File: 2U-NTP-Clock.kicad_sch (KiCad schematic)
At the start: 266 parts, among them Q1 BSS138, Q10 BSS138, Q11 BSS138, Q12 BSS138, Q13 BSS138, Q14 BSS138, Q15 BSS138, Q16 BSS138, Q17 BSS138, Q18 BSS138, Q19 BSS138, Q2 BSS138, Q20 BSS138, Q21 BSS138, Q22 BSS138, Q23 BSS138, Q24 BSS138, Q25 BSS138, Q26 BSS138, Q27 BSS138, Q28 BSS138, Q29 BSS138, Q3 BSS138, Q30 BSS138, Q31 BSS138, Q32 BSS138, Q33 BSS138, Q34 BSS138, Q35 BSS138, Q36 BSS138, Q37 BSS138, Q38 BSS138, Q39 BSS138, Q4 BSS138, Q40 BSS138, Q41 BSS138, Q42 BSS138, Q43 BSS138, Q5 BSS138, Q6 BSS138, Q7 BSS138, Q8 BSS138, Q9 BSS138, U3 74HC595, U4 74HC595, U5 74HC595, U6 74HC595, U7 74HC595, U8 74HC595

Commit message: 仕上げた
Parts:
- added C1: 0.22u, Capacitor_SMD:C_0603_1608Metric, symbol Device:C
- added C2: 0.1u, Capacitor_SMD:C_0603_1608Metric, symbol Device:C
- added D173: D, Diode_SMD:D_SOD-523, symbol Device:D
- added J1: Barrel_Jack_Switch, Connector_BarrelJack:BarrelJack_Horizontal, symbol Connector:Barrel_Jack_Switch
- added U9: L7805, Package_TO_SOT_SMD:TO-252-2, symbol Regulator_Linear:L7805
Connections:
- net +5V: now also C2.1, D173.2 (A), U9.3 (OUT)
- net GND: now also C1.2, C2.2, J1.2, U9.2 (GND)
- new net +12V: C1.1, D173.1 (K), J1.1, J1.3, U9.1 (IN)

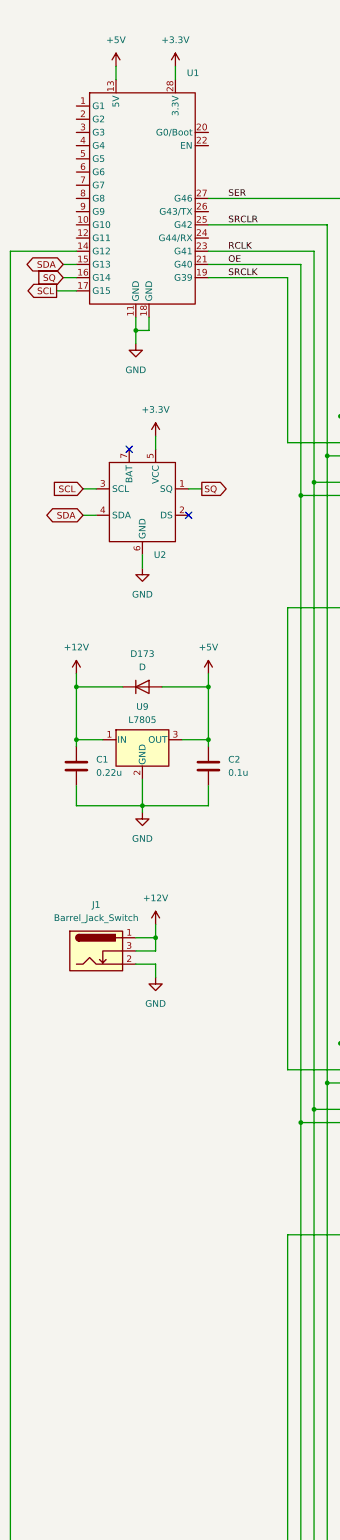
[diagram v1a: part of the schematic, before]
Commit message: スイッチの追加と配置配線修正
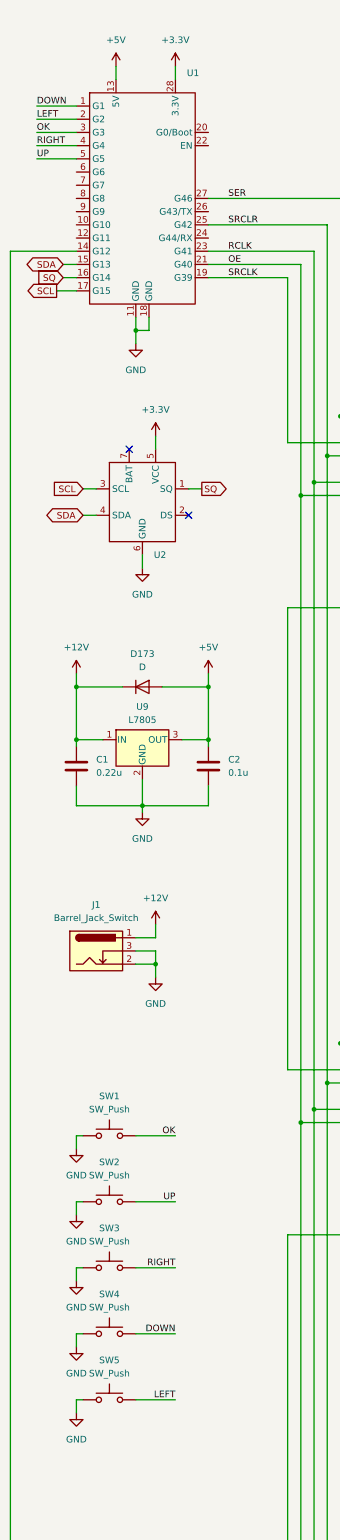
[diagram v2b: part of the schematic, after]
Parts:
- added SW1, SW2, SW3, SW4, SW5: SW_Push, Button_Switch_THT:SW_PUSH_6mm, symbol Switch:SW_Push
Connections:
- net +12V: no longer J1.3
- net GND: now also J1.3, SW1.2, SW2.2, SW3.2, SW4.2, SW5.2
- net DOWN: now reaches U1.1 (G1)
- net DOWN: now also SW4.1
- net LEFT: now reaches U1.2 (G2)
- net LEFT: now also SW5.1
- net OK: now reaches U1.3 (G3)
- net OK: now also SW1.1
- net RIGHT: now reaches U1.4 (G4)
- net RIGHT: now also SW3.1
- net UP: now reaches U1.5 (G5)
- net UP: now also SW2.1

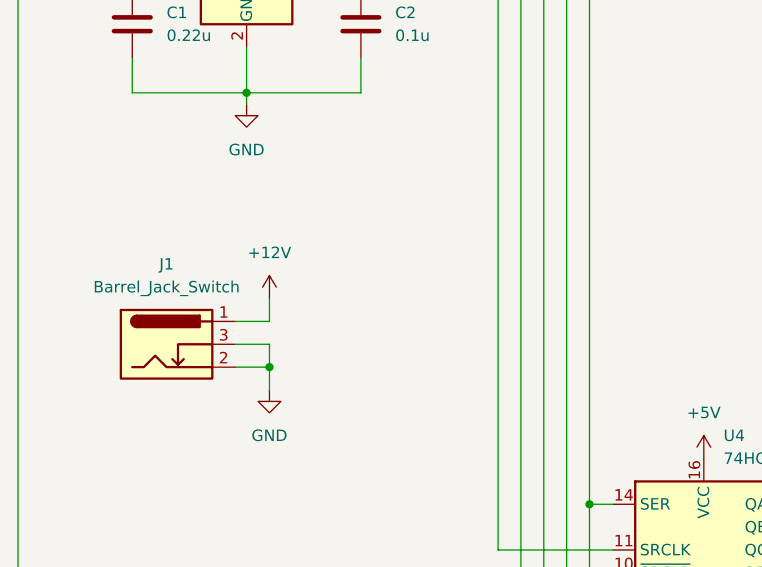
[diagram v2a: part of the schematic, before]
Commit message: わすれてた GND を繋いで製造データ出力
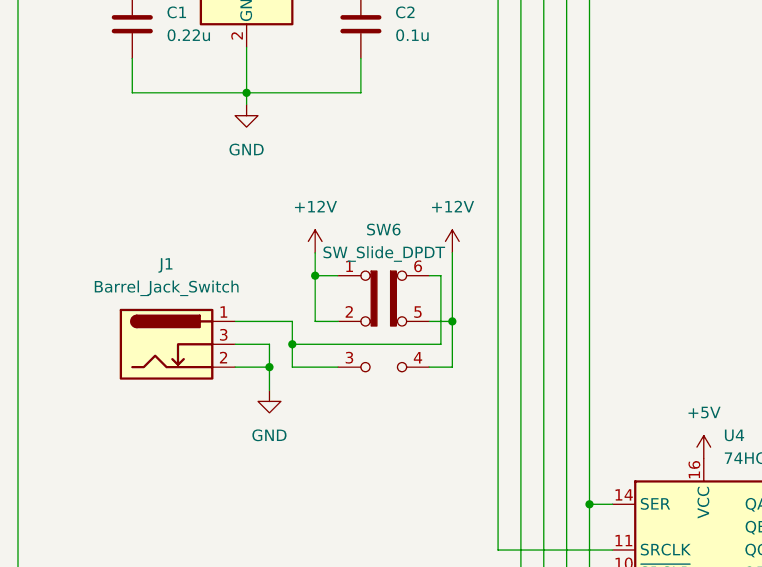
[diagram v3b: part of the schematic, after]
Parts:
- added SW6: SW_Slide_DPDT, Button_Switch_THT:SW_E-Switch_EG1271_SPDT, symbol Switch:SW_Slide_DPDT
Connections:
- net +12V: now also SW6.1 (A), SW6.2 (B), SW6.4 (A), SW6.5 (B); no longer J1.1
- new net: J1.1, SW6.3 (C), SW6.6 (C)
